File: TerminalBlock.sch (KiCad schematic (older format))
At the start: 0 parts

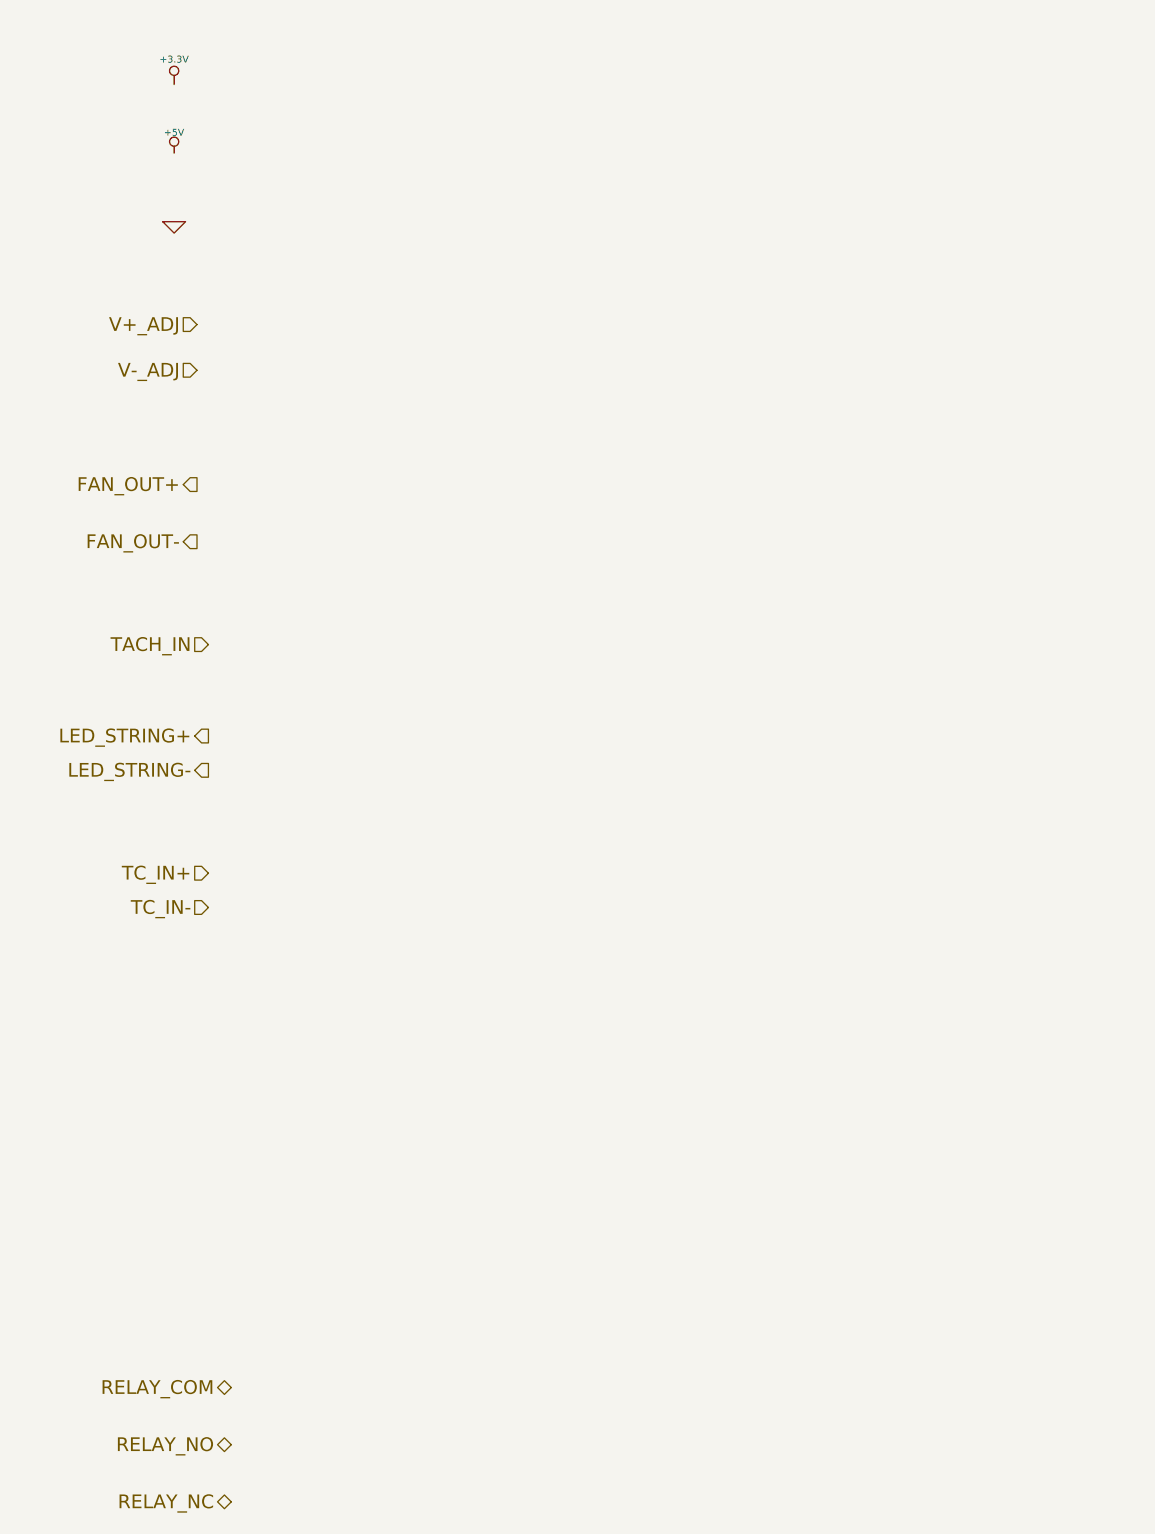
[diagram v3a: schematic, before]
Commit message: Associating the Terminal Blocks
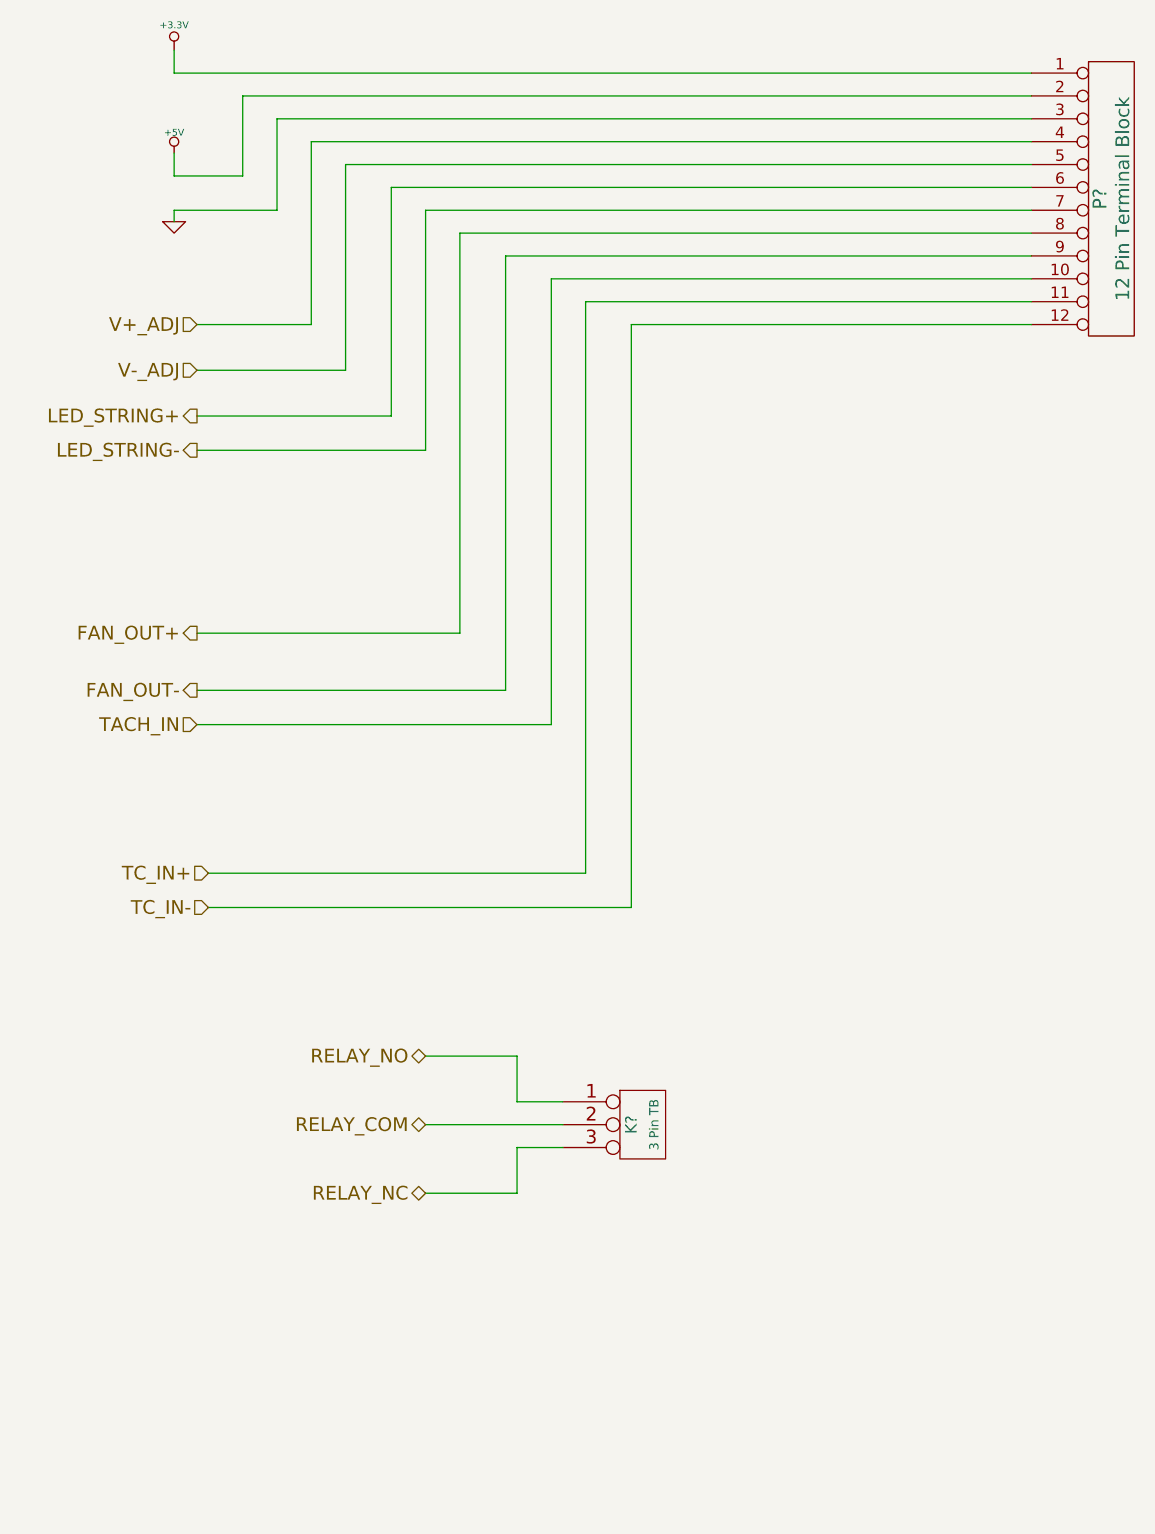
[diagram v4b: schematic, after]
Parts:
- added K?: 3 Pin TB, symbol CONN_3
- added P?: 12 Pin Terminal Block, symbol CONN_12
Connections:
- net +3.3V: now also P?.1 (P1)
- net +5V: now also P?.2 (P2)
- net FAN_OUT+: now also P?.8 (P8)
- net FAN_OUT-: now also P?.9 (P9)
- net GND: now also P?.3 (P3)
- net LED_STRING+: now also P?.6 (P6)
- net LED_STRING-: now also P?.7 (P7)
- net RELAY_COM: now also K?.2 (PM)
- net RELAY_NC: now also K?.3 (P3)
- net RELAY_NO: now also K?.1 (P1)
- net TACH_IN: now also P?.10 (P10)
- net TC_IN+: now also P?.11 (P11)
- net TC_IN-: now also P?.12 (P12)
- net V+_ADJ: now also P?.4 (P4)
- net V-_ADJ: now also P?.5 (P5)
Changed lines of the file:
@@
-EESchema Schematic File Version 2  date 10/11/2013 1:15:54 AM
+EESchema Schematic File Version 2  date 10/11/2013 8:50:27 PM
 LIBS:power
 LIBS:device
@@
 $Descr A4 11693 8268
 encoding utf-8
-Sheet 8 9
+Sheet 9 9
 Title ""
-Date "11 oct 2013"
+Date "12 oct 2013"
 Rev ""
 Comp ""
@@
 Text HLabel 1850 2200 0    60   Input ~ 0
 V-_ADJ
-Text HLabel 1850 2700 0    60   Output ~ 0
+Text HLabel 1850 3350 0    60   Output ~ 0
 FAN_OUT+
-Text HLabel 1850 2950 0    60   Output ~ 0
+Text HLabel 1850 3600 0    60   Output ~ 0
 FAN_OUT-
-Text HLabel 1900 3400 0    60   Input ~ 0
+Text HLabel 1850 3750 0    60   Input ~ 0
 TACH_IN
-Text HLabel 1900 3800 0    60   Output ~ 0
+Text HLabel 1850 2400 0    60   Output ~ 0
 LED_STRING+
-Text HLabel 1900 3950 0    60   Output ~ 0
+Text HLabel 1850 2550 0    60   Output ~ 0
 LED_STRING-
 Text HLabel 1900 4400 0    60   Input ~ 0
@@
 Text HLabel 1900 4550 0    60   Input ~ 0
 TC_IN-
-Text HLabel 2000 6650 0    60   BiDi ~ 0
+Text HLabel 2850 5500 0    60   BiDi ~ 0
 RELAY_COM
-Text HLabel 2000 6900 0    60   BiDi ~ 0
+Text HLabel 2850 5200 0    60   BiDi ~ 0
 RELAY_NO
-Text HLabel 2000 7150 0    60   BiDi ~ 0
+Text HLabel 2850 5800 0    60   BiDi ~ 0
 RELAY_NC
 $Comp
-L +3.3V #PWR058
+L +3.3V #PWR61
 U 1 1 523FFDA7
-P 1750 950
-F 0 "#PWR058" H 1750 910 30  0001 C CNN
-F 1 "+3.3V" H 1750 1060 30  0000 C CNN
-F 2 "~" H 1750 950 60  0000 C CNN
-F 3 "~" H 1750 950 60  0000 C CNN
-	1    1750 950
-	1    0    0    -1
-$EndComp
-$Comp
-L +5V #PWR059
+P 1750 800
+F 0 "#PWR61" H 1750 760 30  0001 C CNN
+F 1 "+3.3V" H 1750 910 30  0000 C CNN
+F 2 "~" H 1750 800 60  0000 C CNN
+F 3 "~" H 1750 800 60  0000 C CNN
+	1    1750 800
+	1    0    0    -1
+$EndComp
+$Comp
+L +5V #PWR62
 U 1 1 523FFDB6
 P 1750 1250
-F 0 "#PWR059" H 1750 1340 20  0001 C CNN
+F 0 "#PWR62" H 1750 1340 20  0001 C CNN
 F 1 "+5V" H 1750 1340 30  0000 C CNN
 F 2 "~" H 1750 1250 60  0000 C CNN
@@
 $EndComp
 $Comp
-L GND #PWR060
+L GND #PWR63
 U 1 1 523FFDC5
 P 1750 1550
-F 0 "#PWR060" H 1750 1550 30  0001 C CNN
+F 0 "#PWR63" H 1750 1550 30  0001 C CNN
 F 1 "GND" H 1750 1480 30  0001 C CNN
 F 2 "~" H 1750 1550 60  0000 C CNN
@@
 	1    0    0    -1
 $EndComp
+$Comp
+L CONN_12 P?
+U 1 1 5258A829
+P 5850 1450
+F 0 "P?" V 5800 1450 60  0000 C CNN
+F 1 "12 Pin Terminal Block" V 5900 1450 60  0000 C CNN
+F 2 "" H 5850 1450 60  0000 C CNN
+F 3 "" H 5850 1450 60  0000 C CNN
+F 4 "On Shore" H 5850 1450 60  0001 C CNN "MFG Name"
+F 5 "OSTTE120104" H 5850 1450 60  0001 C CNN "MFG Part Number"
+	1    5850 1450
+	1    0    0    -1
+$EndComp
+Wire Wire Line
+	5500 900  1750 900
+Wire Wire Line
+	1750 900  1750 800
+Wire Wire Line
+	1750 1250 1750 1350
+Wire Wire Line
+	1750 1350 2050 1350
+Wire Wire Line
+	2050 1350 2050 1000
+Wire Wire Line
+	2050 1000 5500 1000
+Wire Wire Line
+	2200 1100 5500 1100
+Wire Wire Line
+	2200 1100 2200 1500
+Wire Wire Line
+	2200 1500 1750 1500
+Wire Wire Line
+	1750 1500 1750 1550
+Wire Wire Line
+	1850 2000 2350 2000
+Wire Wire Line
+	2350 2000 2350 1200
+Wire Wire Line
+	2350 1200 5500 1200
+Wire Wire Line
+	5500 1300 2500 1300
+Wire Wire Line
+	2500 1300 2500 2200
+Wire Wire Line
+	2500 2200 1850 2200
+Wire Wire Line
+	1850 2400 2700 2400
+Wire Wire Line
+	2700 2400 2700 1400
+Wire Wire Line
+	2700 1400 5500 1400
+Wire Wire Line
+	1850 3350 3000 3350
+Wire Wire Line
+	1850 3600 3200 3600
+Wire Wire Line
+	1850 3750 3400 3750
+Wire Wire Line
+	1850 2550 2850 2550
+Wire Wire Line
+	2850 2550 2850 1500
+Wire Wire Line
+	2850 1500 5500 1500
+Wire Wire Line
+	5500 1600 3000 1600
+Wire Wire Line
+	3000 1600 3000 3350
+Wire Wire Line
+	3200 3600 3200 1700
+Wire Wire Line
+	3200 1700 5500 1700
+Wire Wire Line
+	5500 1800 3400 1800
+Wire Wire Line
+	3400 1800 3400 3750
+Wire Wire Line
+	1900 4400 3550 4400
+Wire Wire Line
+	3550 4400 3550 1900
+Wire Wire Line
+	3550 1900 5500 1900
+Wire Wire Line
+	5500 2000 3750 2000
+Wire Wire Line
+	3750 2000 3750 4550
+Wire Wire Line
+	3750 4550 1900 4550
+$Comp
+L CONN_3 K?
+U 1 1 5258AA07
+P 3800 5500
+F 0 "K?" V 3750 5500 50  0000 C CNN
+F 1 "3 Pin TB" V 3850 5500 40  0000 C CNN
+F 2 "" H 3800 5500 60  0000 C CNN
+F 3 "" H 3800 5500 60  0000 C CNN
+F 4 "Phoenix" H 3800 5500 60  0001 C CNN "MFG Name"
+F 5 "1935174" H 3800 5500 60  0001 C CNN "MFG Part Number"
+	1    3800 5500
+	1    0    0    -1
+$EndComp
+Wire Wire Line
+	3450 5500 2850 5500
+Wire Wire Line
+	2850 5200 3250 5200
+Wire Wire Line
+	3250 5200 3250 5400
+Wire Wire Line
+	3250 5400 3450 5400
+Wire Wire Line
+	3450 5600 3250 5600
+Wire Wire Line
+	3250 5600 3250 5800
+Wire Wire Line
+	3250 5800 2850 5800
 $EndSCHEMATC

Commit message: Placing the Terminal Block/ATX Connectors
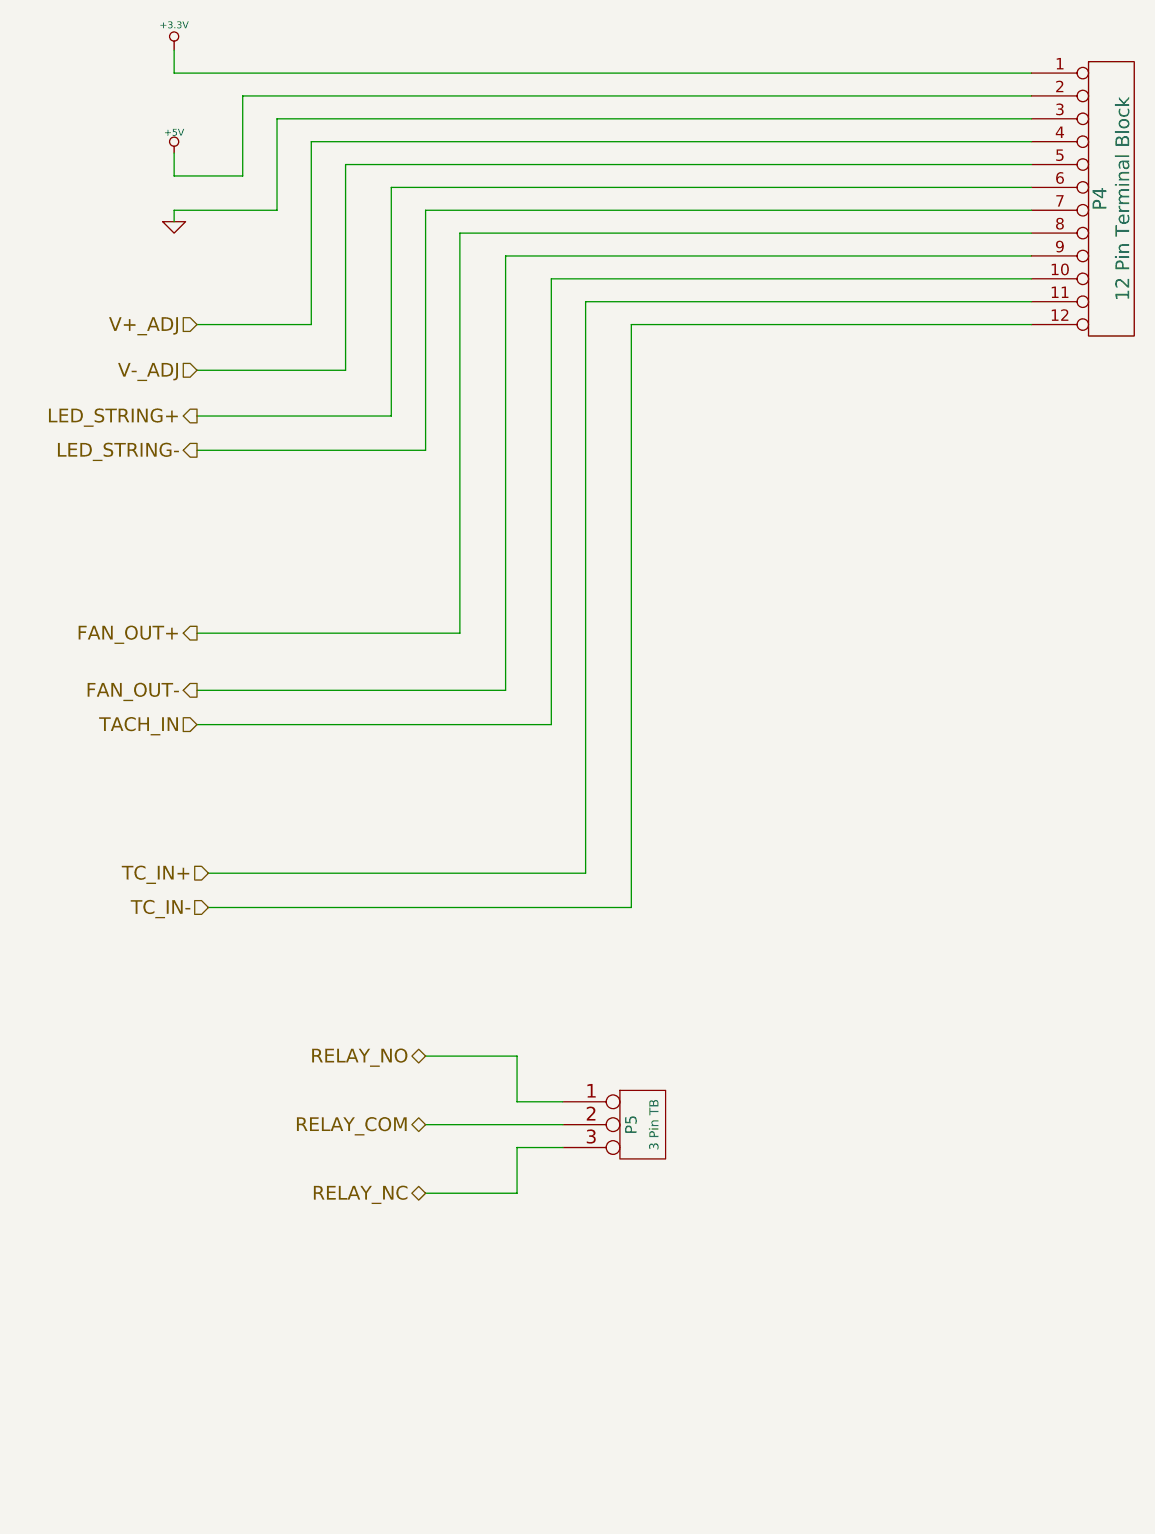
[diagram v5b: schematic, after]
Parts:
- gave numbers to parts that had none: 2
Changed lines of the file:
@@
-EESchema Schematic File Version 2  date 10/11/2013 8:50:27 PM
+EESchema Schematic File Version 2  date 10/11/2013 9:16:27 PM
 LIBS:power
 LIBS:device
@@
 $EndComp
 $Comp
-L CONN_12 P?
+L CONN_12 P4
 U 1 1 5258A829
 P 5850 1450
-F 0 "P?" V 5800 1450 60  0000 C CNN
+F 0 "P4" V 5800 1450 60  0000 C CNN
 F 1 "12 Pin Terminal Block" V 5900 1450 60  0000 C CNN
 F 2 "" H 5850 1450 60  0000 C CNN
@@
 	3750 4550 1900 4550
 $Comp
-L CONN_3 K?
+L CONN_3 P5
 U 1 1 5258AA07
 P 3800 5500
-F 0 "K?" V 3750 5500 50  0000 C CNN
+F 0 "P5" V 3750 5500 50  0000 C CNN
 F 1 "3 Pin TB" V 3850 5500 40  0000 C CNN
 F 2 "" H 3800 5500 60  0000 C CNN
